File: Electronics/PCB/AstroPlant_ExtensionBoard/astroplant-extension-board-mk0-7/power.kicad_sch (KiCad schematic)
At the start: 13 parts, among them J14 61300621121, J20 Conn_01x02, J21 Conn_01x02

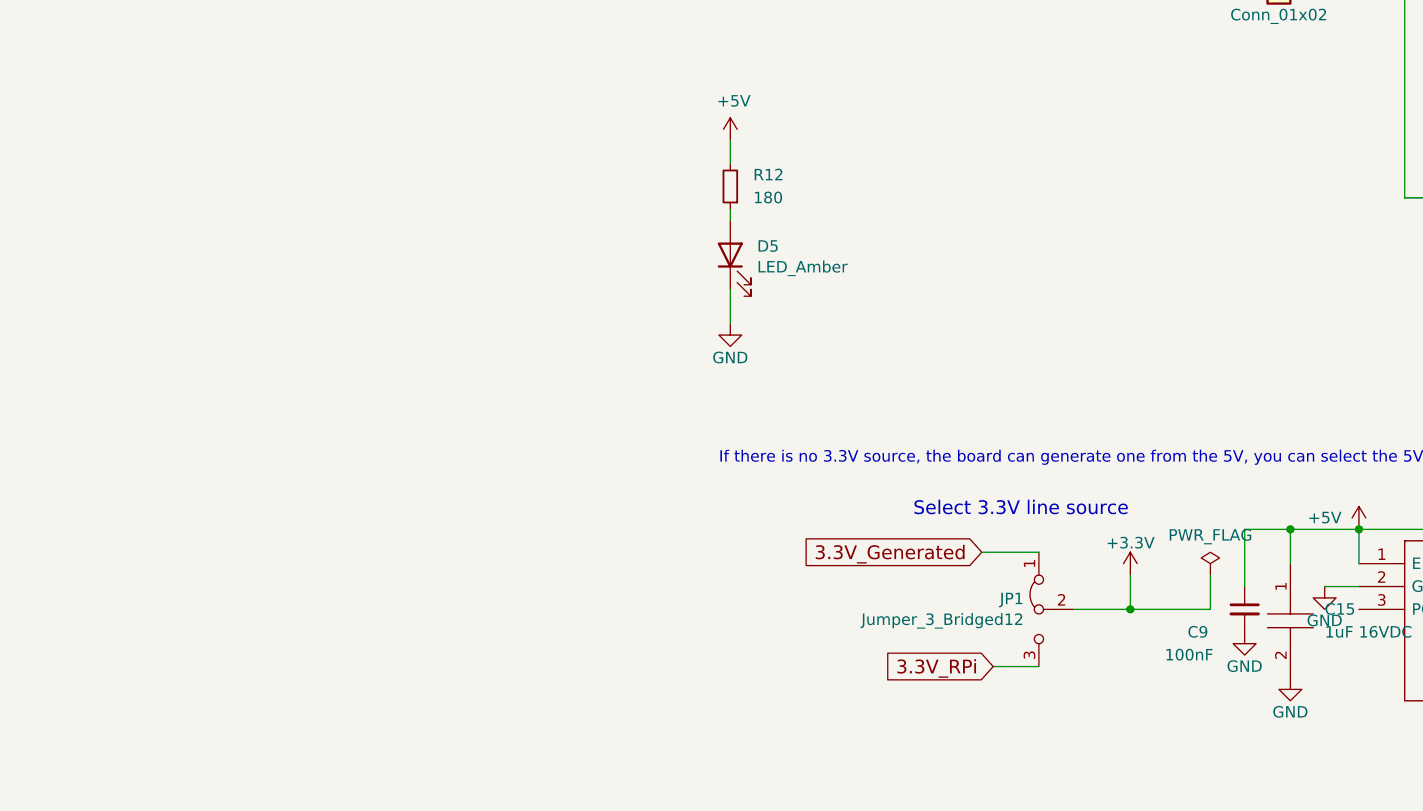
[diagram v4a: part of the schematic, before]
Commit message: Changed PCB, add a LED to simplify tests
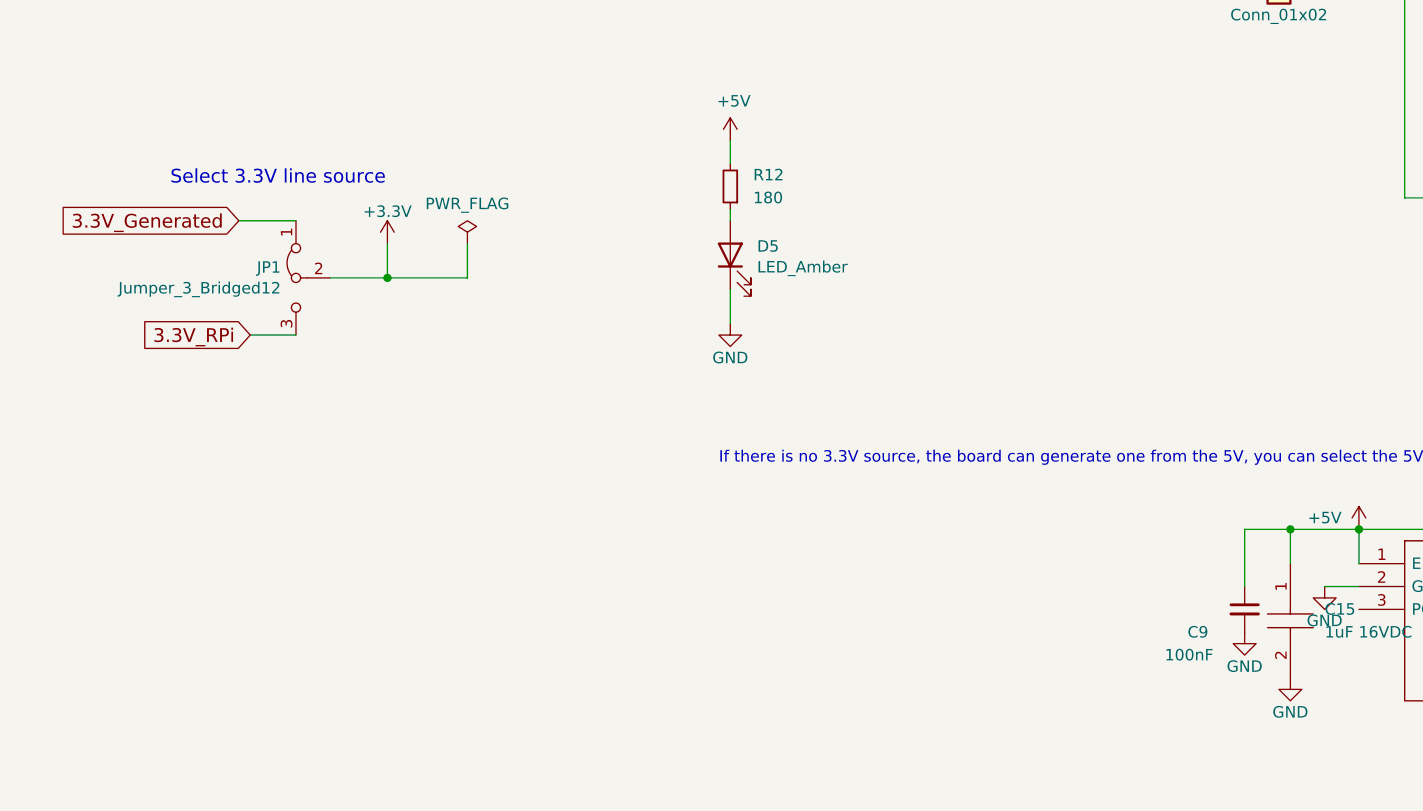
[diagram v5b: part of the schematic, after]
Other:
- moved on the sheet: JP1
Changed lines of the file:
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@@
   (title_block
     (title "Power management")
-    (date "2018-02-13")
-    (rev "0.5")
-    (comment 1 "Vincent Frangi")
-    (comment 2 "vincent.frangi@gmail.com")
+    (date "2023-10-13")
+    (rev "0.7")
+    (comment 1 "Aurélien Lesage")
   )
   (junction (at 180.34 135.89) (diameter 0) (color 0 0 0 0)
@@
   (junction (at 223.52 99.06) (diameter 0) (color 0 0 0 0)
   )
-  (junction (at 162.56 144.78) (diameter 0) (color 0 0 0 0)
+  (junction (at 80.01 107.95) (diameter 0) (color 0 0 0 0)
   )
   (junction (at 187.96 135.89) (diameter 0) (color 0 0 0 0)
@@
     (stroke (width 0) (type default))
   )
-  (wire (pts (xy 147.32 151.13) (xy 152.4 151.13))
+  (wire (pts (xy 64.77 114.3) (xy 69.85 114.3))
     (stroke (width 0) (type default))
   )
@@
     (stroke (width 0) (type default))
   )
-  (wire (pts (xy 171.45 140.97) (xy 171.45 144.78))
+  (wire (pts (xy 88.9 104.14) (xy 88.9 107.95))
     (stroke (width 0) (type default))
   )
@@
     (stroke (width 0) (type default))
   )
-  (wire (pts (xy 156.21 144.78) (xy 162.56 144.78))
+  (wire (pts (xy 73.66 107.95) (xy 80.01 107.95))
     (stroke (width 0) (type default))
   )
@@
     (stroke (width 0) (type default))
   )
-  (wire (pts (xy 146.05 138.43) (xy 152.4 138.43))
+  (wire (pts (xy 63.5 101.6) (xy 69.85 101.6))
     (stroke (width 0) (type default))
   )
@@
     (stroke (width 0) (type default))
   )
-  (wire (pts (xy 162.56 144.78) (xy 162.56 140.97))
+  (wire (pts (xy 80.01 107.95) (xy 80.01 104.14))
     (stroke (width 0) (type default))
   )
@@
     (stroke (width 0) (type default))
   )
-  (wire (pts (xy 171.45 144.78) (xy 162.56 144.78))
+  (wire (pts (xy 88.9 107.95) (xy 80.01 107.95))
     (stroke (width 0) (type default))
   )
@@
     (effects (font (size 1.524 1.524)) (justify left bottom))
   )
-  (text "Select 3.3V line source" (at 138.43 134.62 0)
+  (text "Select 3.3V line source" (at 55.88 97.79 0)
     (effects (font (size 1.524 1.524)) (justify left bottom))
   )
@@
     )
   )
-  (global_label "3.3V_RPi" (shape input) (at 147.32 151.13 180)
+  (global_label "3.3V_RPi" (shape input) (at 64.77 114.3 180)
     (effects (font (size 1.524 1.524)) (justify right))
-    (property "Intersheetrefs" "${INTERSHEET_REFS}" (at 147.32 151.13 0)
+    (property "Intersheetrefs" "${INTERSHEET_REFS}" (at 64.77 114.3 0)
       (effects (font (size 1.27 1.27)) hide)
     )
@@
     )
   )
-  (global_label "3.3V_Generated" (shape input) (at 146.05 138.43 180)
+  (global_label "3.3V_Generated" (shape input) (at 63.5 101.6 180)
     (effects (font (size 1.524 1.524)) (justify right))
-    (property "Intersheetrefs" "${INTERSHEET_REFS}" (at 146.05 138.43 0)
+    (property "Intersheetrefs" "${INTERSHEET_REFS}" (at 63.5 101.6 0)
       (effects (font (size 1.27 1.27)) hide)
     )
@@
     )
   )
-  (symbol (lib_id "Astroplant_VFR-rescue:Jumper_3_Bridged12-Jumper") (at 152.4 144.78 90) (mirror x) (unit 1)
-    (in_bom yes) (on_board yes) (dnp no)
-    (property "Reference" "JP1" (at 150.7236 143.6116 90)
+  (symbol (lib_id "Astroplant_VFR-rescue:Jumper_3_Bridged12-Jumper") (at 69.85 107.95 90) (mirror x) (unit 1)
+    (in_bom yes) (on_board yes) (dnp no)
+    (property "Reference" "JP1" (at 68.1736 106.7816 90)
       (effects (font (size 1.27 1.27)) (justify left))
     )
-    (property "Value" "Jumper_3_Bridged12" (at 150.7236 145.923 90)
+    (property "Value" "Jumper_3_Bridged12" (at 68.1736 109.093 90)
       (effects (font (size 1.27 1.27)) (justify left))
     )
-    (property "Footprint" "Connector_PinHeader_2.54mm:PinHeader_1x03_P2.54mm_Vertical" (at 152.4 144.78 0)
-      (effects (font (size 1.27 1.27)) hide)
-    )
-    (property "Datasheet" "http://katalog.we-online.de/em/datasheet/6130xx11121.pdf" (at 152.4 144.78 0)
-      (effects (font (size 1.27 1.27)) hide)
-    )
-    (property "MPN" "61300311121" (at 152.4 144.78 0)
-      (effects (font (size 1.27 1.27)) hide)
-    )
-    (property "Digikey PN" "732-5316-ND" (at 152.4 144.78 0)
+    (property "Footprint" "Connector_PinHeader_2.54mm:PinHeader_1x03_P2.54mm_Vertical" (at 69.85 107.95 0)
+      (effects (font (size 1.27 1.27)) hide)
+    )
+    (property "Datasheet" "http://katalog.we-online.de/em/datasheet/6130xx11121.pdf" (at 69.85 107.95 0)
+      (effects (font (size 1.27 1.27)) hide)
+    )
+    (property "MPN" "61300311121" (at 69.85 107.95 0)
+      (effects (font (size 1.27 1.27)) hide)
+    )
+    (property "Digikey PN" "732-5316-ND" (at 69.85 107.95 0)
       (effects (font (size 1.27 1.27)) hide)
     )
@@
     )
   )
-  (symbol (lib_id "power:PWR_FLAG") (at 171.45 140.97 0) (unit 1)
-    (in_bom yes) (on_board yes) (dnp no)
-    (property "Reference" "#FLG0105" (at 171.45 139.065 0)
-      (effects (font (size 1.27 1.27)) hide)
-    )
-    (property "Value" "PWR_FLAG" (at 171.45 136.5504 0)
-      (effects (font (size 1.27 1.27)))
-    )
-    (property "Footprint" "" (at 171.45 140.97 0)
-      (effects (font (size 1.27 1.27)) hide)
-    )
-    (property "Datasheet" "~" (at 171.45 140.97 0)
+  (symbol (lib_id "power:PWR_FLAG") (at 88.9 104.14 0) (unit 1)
+    (in_bom yes) (on_board yes) (dnp no)
+    (property "Reference" "#FLG0105" (at 88.9 102.235 0)
+      (effects (font (size 1.27 1.27)) hide)
+    )
+    (property "Value" "PWR_FLAG" (at 88.9 99.7204 0)
+      (effects (font (size 1.27 1.27)))
+    )
+    (property "Footprint" "" (at 88.9 104.14 0)
+      (effects (font (size 1.27 1.27)) hide)
+    )
+    (property "Datasheet" "~" (at 88.9 104.14 0)
       (effects (font (size 1.27 1.27)) hide)
     )
@@
     )
   )
-  (symbol (lib_id "Astroplant_VFR-rescue:+3.3V-power") (at 162.56 140.97 0) (unit 1)
-    (in_bom yes) (on_board yes) (dnp no)
-    (property "Reference" "#PWR0116" (at 162.56 144.78 0)
-      (effects (font (size 1.27 1.27)) hide)
-    )
-    (property "Value" "+3.3V" (at 162.56 137.414 0)
-      (effects (font (size 1.27 1.27)))
-    )
-    (property "Footprint" "" (at 162.56 140.97 0)
-      (effects (font (size 1.27 1.27)) hide)
-    )
-    (property "Datasheet" "" (at 162.56 140.97 0)
-      (effects (font (size 1.27 1.27)) hide)
-    )
+  (symbol (lib_id "Astroplant_VFR-rescue:+3.3V-power") (at 80.01 104.14 0) (unit 1)
+    (in_bom yes) (on_board yes) (dnp no)
+    (property "Reference" "#PWR0116" (at 80.01 107.95 0)
+      (effects (font (size 1.27 1.27)) hide)
+    )
+    (property "Value" "+3.3V" (at 80.01 100.584 0)
+      (effects (font (size 1.27 1.27)))
+    )
+    (property "Footprint" "" (at 80.01 104.14 0)
+      (effects (font (size 1.27 1.27)) hide)
+    )
+    (property "Datasheet" "" (at 80.01 104.14 0)
+      (effects (font (size 1.27 1.27)) hide)
+    )

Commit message: Updated PCB from a backup save to solve issue with git
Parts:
- C15, C16: value 1uF 16VDC -> GRM185R61C105KE44D
- C3: value 470uF -> 875115150005
- C9: value 100nF -> VJ0603Y104MXJCW1BC
- D5: value LED_Amber -> SML-D12D8WT8
- J20, J21: value Conn_01x02 -> 691102710002
- JP1: value Jumper_3_Bridged12 -> 61300311121
- R12: value 180 -> CRCW0603180RFKEA
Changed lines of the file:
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@@
       (effects (font (size 1.27 1.27)))
     )
-    (property "Value" "Conn_01x02" (at 179.07 78.74 0)
+    (property "Value" "691102710002" (at 179.07 78.74 0)
       (effects (font (size 1.27 1.27)))
     )
@@
       (effects (font (size 1.27 1.27)))
     )
-    (property "Value" "Conn_01x02" (at 66.04 67.31 0)
+    (property "Value" "691102710002" (at 66.04 67.31 0)
       (effects (font (size 1.27 1.27)))
     )
@@
       (effects (font (size 1.27 1.27)) (justify left))
     )
-    (property "Value" "470uF" (at 91.2368 67.183 0)
+    (property "Value" "875115150005" (at 91.2368 67.183 0)
       (effects (font (size 1.27 1.27)) (justify left))
     )
@@
       (effects (font (size 1.27 1.27)) (justify right))
     )
-    (property "Value" "LED_Amber" (at 121.0818 106.7562 90)
+    (property "Value" "SML-D12D8WT8" (at 121.0818 106.7562 90)
       (effects (font (size 1.27 1.27)) (justify right))
     )
@@
       (effects (font (size 1.27 1.27)) (justify left))
     )
-    (property "Value" "100nF" (at 246.38 148.5963 0)
+    (property "Value" "VJ0603Y104MXJCW1BC" (at 246.38 148.5963 0)
       (effects (font (size 1.27 1.27)) (justify left))
     )
@@
       (effects (font (size 1.27 1.27)) (justify left))
     )
-    (property "Value" "Jumper_3_Bridged12" (at 68.1736 109.093 90)
+    (property "Value" "61300311121" (at 68.1736 109.093 90)
       (effects (font (size 1.27 1.27)) (justify left))
     )
@@
       (effects (font (size 1.27 1.27)) (justify left))
     )
-    (property "Value" "1uF 16VDC" (at 233.68 152.4 90)
+    (property "Value" "GRM185R61C105KE44D" (at 233.68 152.4 90)
       (effects (font (size 1.27 1.27)) (justify left))
     )
@@
       (effects (font (size 1.27 1.27)) (justify right))
     )
-    (property "Value" "180" (at 120.65 99.06 0)
+    (property "Value" "CRCW0603180RFKEA" (at 120.65 99.06 0)
       (effects (font (size 1.27 1.27)) (justify right))
     )
@@
       (effects (font (size 1.27 1.27)) (justify left))
     )
-    (property "Value" "100nF" (at 166.37 149.86 0)
+    (property "Value" "VJ0603Y104MXJCW1BC" (at 166.37 149.86 0)
       (effects (font (size 1.27 1.27)) (justify left))
     )
@@
       (effects (font (size 1.27 1.27)) (justify left))
     )
-    (property "Value" "1uF 16VDC" (at 184.15 147.32 90)
-      (effects (font (size 1.27 1.27)) (justify left))
-    )
+    (property "Value" "GRM185R61C105KE44D" (at 184.15 147.32 90)
+      (effects (font (size 1.27 1.27)) (justify left))
+    )

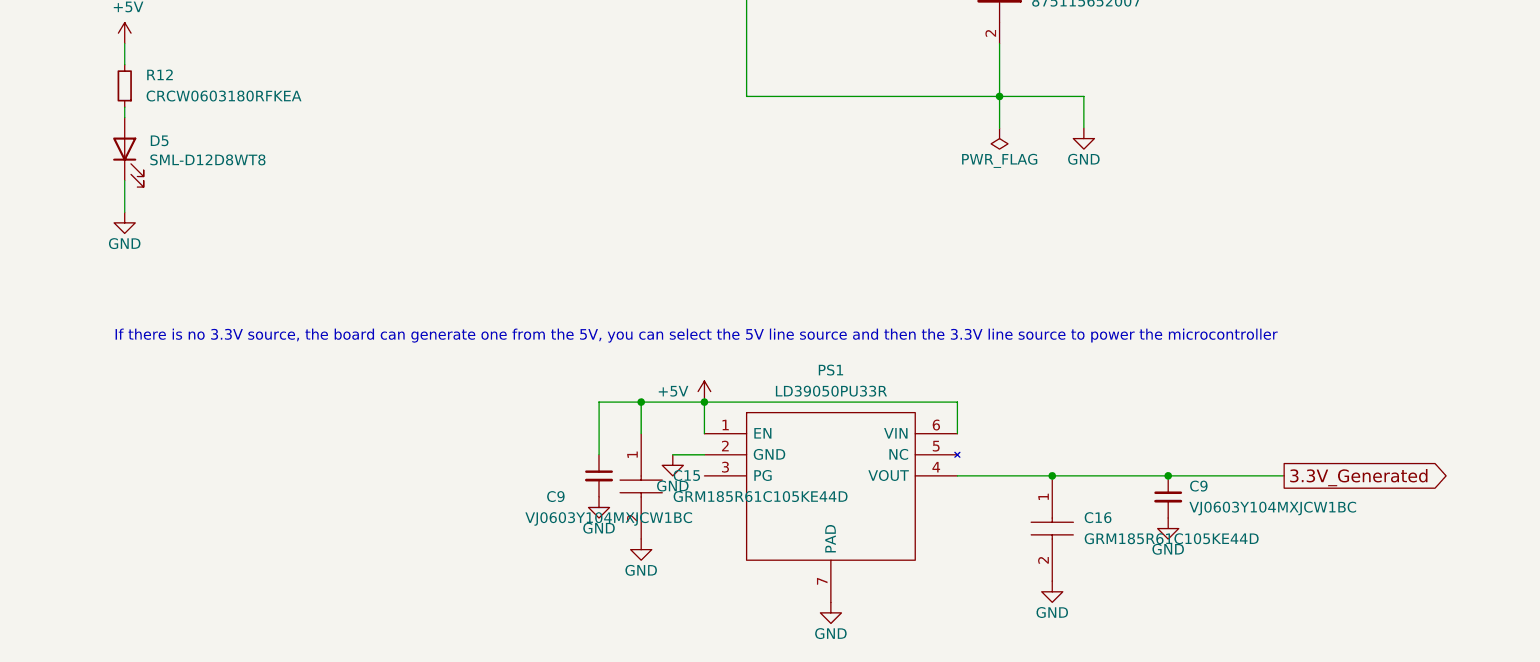
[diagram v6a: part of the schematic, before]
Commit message: Last commit (software + hardware change)
hardware : updated readme, change pcb to solve the issues of the 1st prototype
software : add code (to create a zigbee network)
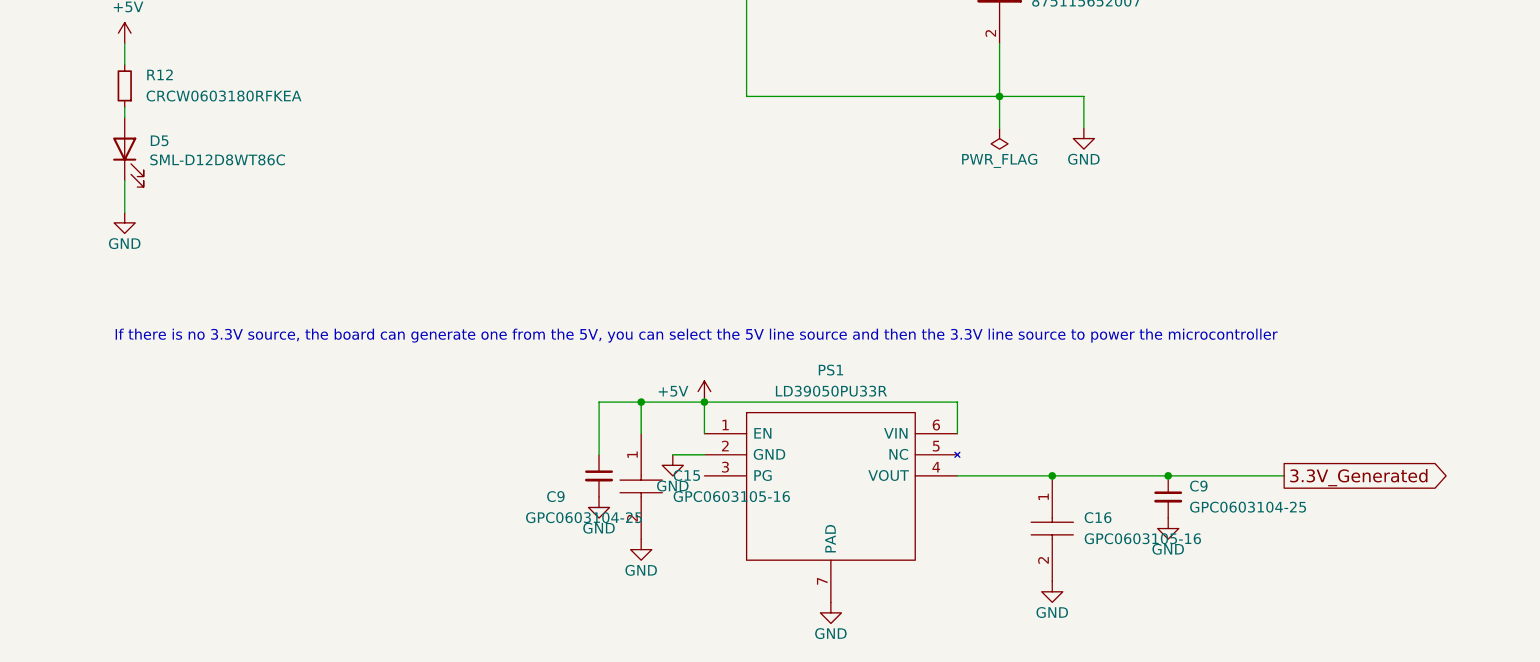
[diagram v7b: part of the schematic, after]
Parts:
- C15, C16: value GRM185R61C105KE44D -> GPC0603105-16; Capacitance (none) -> 1uF
- C3: Capacitance (none) -> 470uF
- C4: Capacitance (none) -> 100uF
- C9: value VJ0603Y104MXJCW1BC -> GPC0603104-25; Capacitance (none) -> 100nF; MPN VJ0603Y104MXJCW1BC -> GPC0603104-25
- D5: value SML-D12D8WT8 -> SML-D12D8WT86C; MPN SML-D12D8WT8 -> SML-D12D8WT86C; Manufacturer_Part_Number (none) -> SML-D12D8WT86C
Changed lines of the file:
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@@
+      (effects (font (size 1.27 1.27)) hide)
+    )
+    (property "Capacitance" "470uF" (at 88.9 66.04 0)
       (effects (font (size 1.27 1.27)) hide)
     )
@@
       (effects (font (size 1.27 1.27)) (justify right))
     )
-    (property "Value" "SML-D12D8WT8" (at 121.0818 106.7562 90)
+    (property "Value" "SML-D12D8WT86C" (at 121.0818 106.7562 90)
       (effects (font (size 1.27 1.27)) (justify right))
     )
@@
       (effects (font (size 1.27 1.27)) hide)
     )
-    (property "MPN" "SML-D12D8WT8" (at 118.11 105.41 0)
+    (property "MPN" "SML-D12D8WT86C" (at 118.11 105.41 0)
       (effects (font (size 1.27 1.27)) hide)
     )
     (property "Mouser PN" " 755-SML-D12D8WT86C" (at 118.11 105.41 0)
+      (effects (font (size 1.27 1.27)) hide)
+    )
+    (property "Manufacturer_Part_Number" "SML-D12D8WT86C" (at 118.11 105.41 0)
       (effects (font (size 1.27 1.27)) hide)
     )
@@
       (effects (font (size 1.27 1.27)) hide)
     )
+    (property "Capacitance" "100uF" (at 223.52 80.01 0)
+      (effects (font (size 1.27 1.27)) hide)
+    )
     (pin "1")
     (pin "2")
@@
       (effects (font (size 1.27 1.27)) (justify left))
     )
-    (property "Value" "VJ0603Y104MXJCW1BC" (at 246.38 148.5963 0)
+    (property "Value" "GPC0603104-25 " (at 246.38 148.5963 0)
       (effects (font (size 1.27 1.27)) (justify left))
     )
@@
       (effects (font (size 1.27 1.27)) hide)
     )
-    (property "MPN" "VJ0603Y104MXJCW1BC" (at 243.84 147.32 0)
+    (property "MPN" "GPC0603104-25 " (at 243.84 147.32 0)
+      (effects (font (size 1.27 1.27)) hide)
+    )
+    (property "Capacitance" "100nF" (at 243.84 147.32 0)
       (effects (font (size 1.27 1.27)) hide)
     )
@@
       (effects (font (size 1.27 1.27)) (justify left))
     )
-    (property "Value" "GRM185R61C105KE44D" (at 233.68 152.4 90)
+    (property "Value" "GPC0603105-16" (at 233.68 152.4 90)
       (effects (font (size 1.27 1.27)) (justify left))
     )
@@
     (property "Arrow Price/Stock" "https://www.arrow.com/en/products/grm185r61c105ke44d/murata-manufacturing" (at 208.28 153.67 0)
       (effects (font (size 1.27 1.27)) (justify left) hide)
+    )
+    (property "Capacitance" "1uF" (at 229.87 144.78 0)
+      (effects (font (size 1.27 1.27)) hide)
     )
     (pin "1")
@@
       (effects (font (size 1.27 1.27)) (justify left))
     )
-    (property "Value" "VJ0603Y104MXJCW1BC" (at 166.37 149.86 0)
+    (property "Value" "GPC0603104-25 " (at 166.37 149.86 0)
       (effects (font (size 1.27 1.27)) (justify left))
     )
@@
       (effects (font (size 1.27 1.27)) hide)
     )
-    (property "MPN" "VJ0603Y104MXJCW1BC" (at 175.26 144.78 0)
+    (property "MPN" "GPC0603104-25 " (at 175.26 144.78 0)
+      (effects (font (size 1.27 1.27)) hide)
+    )
+    (property "Capacitance" "100nF" (at 175.26 144.78 0)
       (effects (font (size 1.27 1.27)) hide)
     )
@@
       (effects (font (size 1.27 1.27)) (justify left))
     )
-    (property "Value" "GRM185R61C105KE44D" (at 184.15 147.32 90)
+    (property "Value" "GPC0603105-16" (at 184.15 147.32 90)
       (effects (font (size 1.27 1.27)) (justify left))
     )
@@
       (effects (font (size 1.27 1.27)) (justify left) hide)
     )
-    (pin "1")
+    (property "Capacitance" "1uF" (at 180.34 139.7 0)
+      (effects (font (size 1.27 1.27)) hide)
+    )
+    (pin "1")
